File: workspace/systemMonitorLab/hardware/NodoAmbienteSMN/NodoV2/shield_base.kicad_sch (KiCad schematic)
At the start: 18 parts, among them J1 Molex_MainBoard_DHT22, J2 Molex_MainBoard_BMP280, J3 Jack-DC, J6 Molex_MainBoard_Led_Status, Q1 Q_NPN_BEC, Q2 Q_NPN_BEC, Q3 Q_NPN_BEC, Q4 Q_NPN_BEC, U1 NodeMcuEsp8266

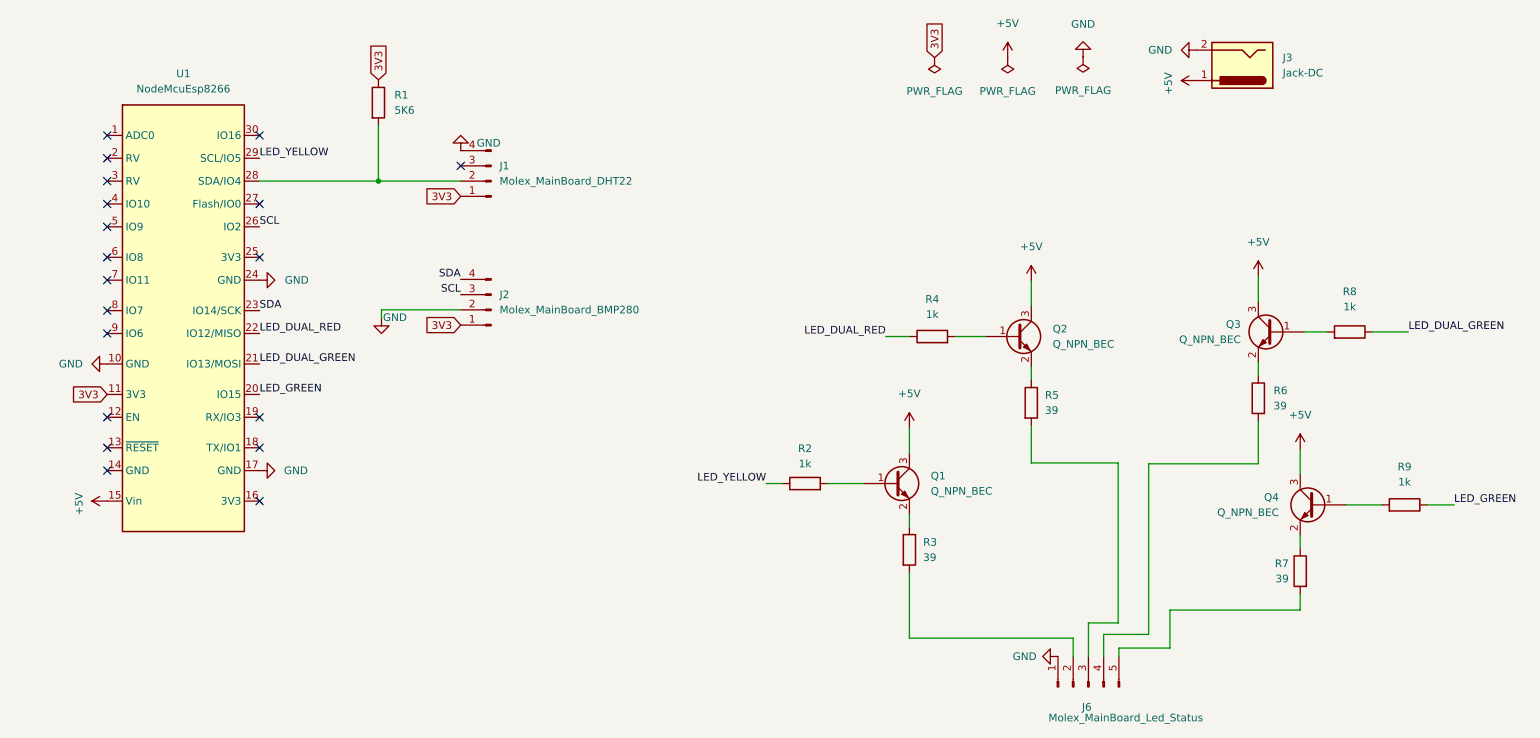
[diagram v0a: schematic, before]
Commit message: Se termino de generar el diseño de la placa shield_main_board.
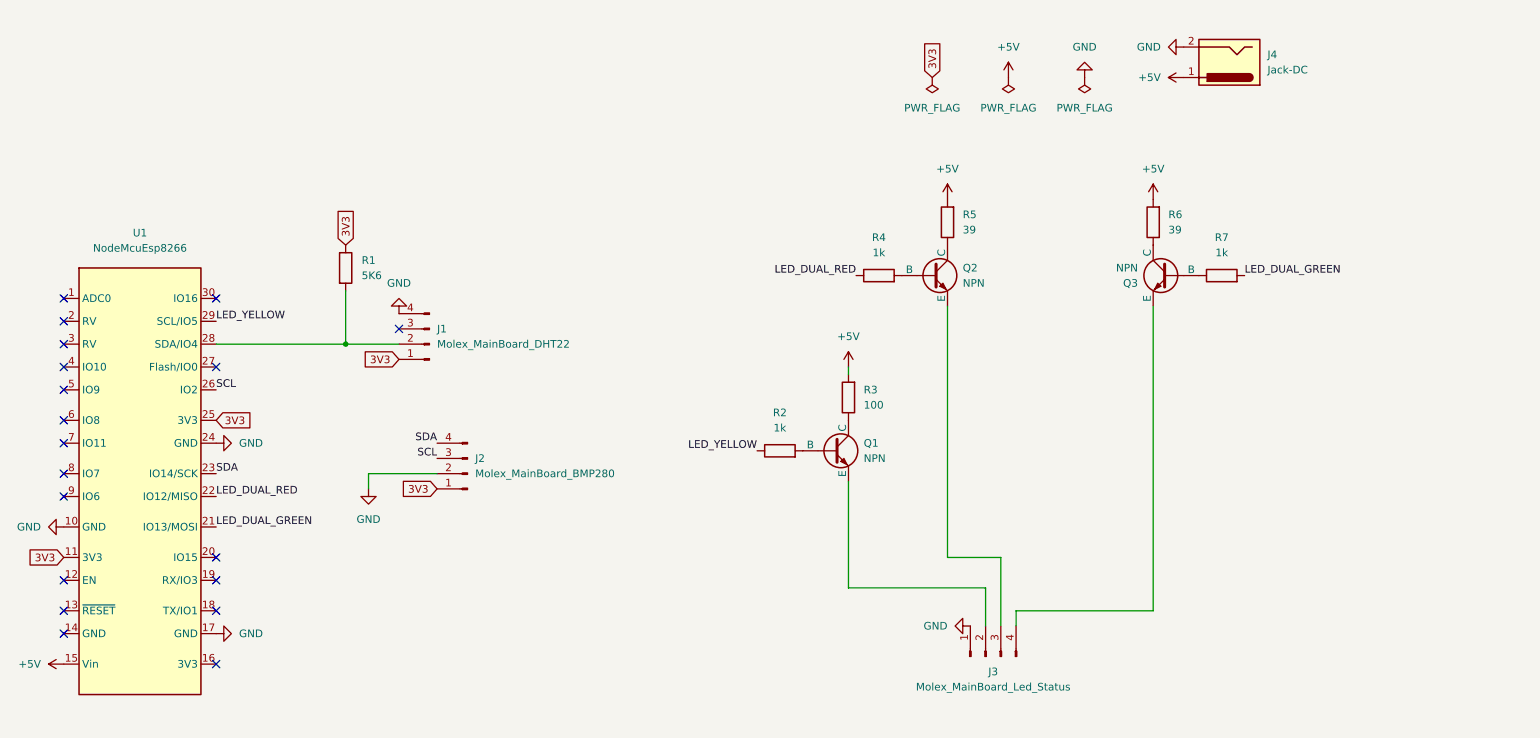
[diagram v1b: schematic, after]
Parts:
- removed J1: Molex_MainBoard_DHT22, Connector_PinHeader_2.54mm:PinHeader_1x04_P2.54mm_Horizontal, symbol Connector:Conn_01x04_Male
- removed J2: Molex_MainBoard_BMP280, Connector_PinHeader_2.54mm:PinHeader_1x04_P2.54mm_Horizontal, symbol Connector:Conn_01x04_Male
- removed J3: Jack-DC, Connector_BarrelJack:BarrelJack_GCT_DCJ200-10-A_Horizontal, symbol Connector:Jack-DC
- removed J6: Molex_MainBoard_Led_Status, Connector_PinHeader_2.54mm:PinHeader_1x05_P2.54mm_Horizontal, symbol Connector:Conn_01x05_Male
- removed Q1, Q2, Q3, Q4: Q_NPN_BEC, Package_TO_SOT_SMD:SOT-23, symbol Device:Q_NPN_BEC
- removed R8, R9: 1k, Resistor_SMD:R_1206_3216Metric, symbol Device:R
- removed U1: NodeMcuEsp8266, NodeMCU_Module:ESP8266_v3, symbol New_Library:NodeMcuEsp8266
- added J1: Molex_MainBoard_DHT22, Connector_PinHeader_2.54mm:PinHeader_1x04_P2.54mm_Horizontal, symbol Connector:Conn_01x04_Pin
- added J2: Molex_MainBoard_BMP280, Connector_PinHeader_2.54mm:PinHeader_1x04_P2.54mm_Horizontal, symbol Connector:Conn_01x04_Pin
- added J3: Molex_MainBoard_Led_Status, Connector_PinHeader_2.54mm:PinHeader_1x04_P2.54mm_Horizontal, symbol Connector:Conn_01x04_Pin
- added J4: Jack-DC, Connector_BarrelJack:BarrelJack_Horizontal, symbol Connector:Jack-DC
- added Q1, Q2, Q3: NPN, Package_TO_SOT_SMD:SOT-23, symbol Simulation_SPICE:NPN
- added U1: NodeMcuEsp8266, Module_commercial:ESP8266_v3, symbol Modulos_comerciales:NodeMcuEsp8266
- R3: value 39 -> 100
- R7: value 39 -> 1k
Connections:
- net +5V: now also R3.2, R5.2, R6.2, J4.1, U1.15 (Vin)
- net 3V3: now also J1.1 (Pin_1), J2.1 (Pin_1), U1.11 (3V3), U1.25 (3V3)
- net GND: now also J1.4 (Pin_4), J2.2 (Pin_2), J3.1 (Pin_1), J4.2, U1.10 (GND), U1.17 (GND), U1.24 (GND)
- net LED_DUAL_GREEN: now also R7.2, U1.21 (IO13/MOSI)
- net LED_DUAL_RED: now also U1.22 (IO12/MISO)
- net LED_YELLOW: now also U1.29 (SCL/IO5)
- net SCL: now also J2.3 (Pin_3), U1.26 (IO2)
- net SDA: now also J2.4 (Pin_4), U1.23 (IO14/SCK)
- net at R3.1: now also Q1.1 (C)
- net at R7.1: now also Q3.2 (B)
- net at R6.1: now also Q3.1 (C)
- net at R4.2: now also Q2.2 (B)
- net at R1.2: now also J1.2 (Pin_2), U1.28 (SDA/IO4)
- net at R5.1: now also Q2.1 (C)
- net at R2.2: now also Q1.2 (B)
- new net: J3.4 (Pin_4), Q3.3 (E)
- new net: J3.3 (Pin_3), Q2.3 (E)
- new net: J3.2 (Pin_2), Q1.3 (E)
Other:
- company: Servicio Meteorologico Argentino (SMN) -> Servicio Meteorológico Nacional (SMN)
- moved on the sheet: R1

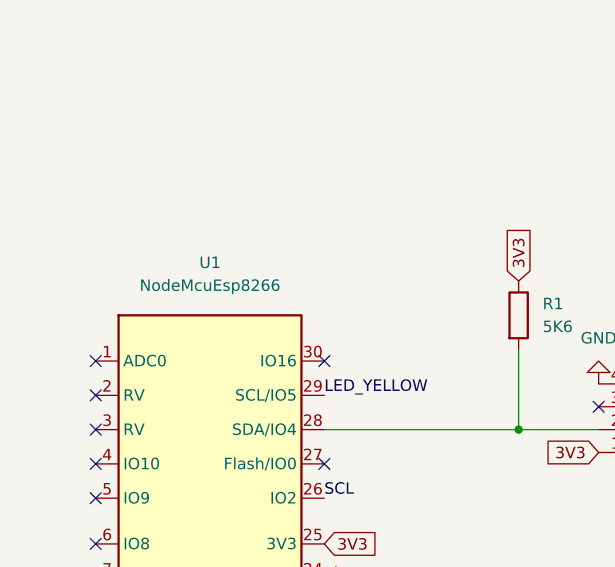
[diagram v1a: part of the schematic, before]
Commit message: Actulizamos pcbs de nodo ambiente v2
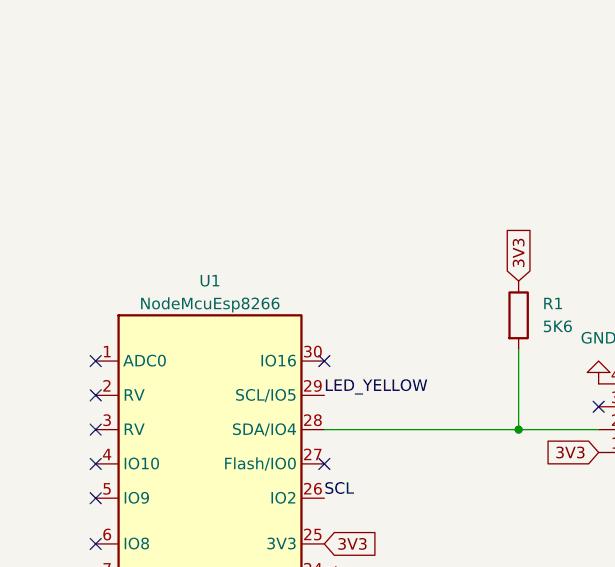
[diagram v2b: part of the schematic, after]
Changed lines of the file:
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@@
 		(fields_autoplaced yes)
 		(property "Reference" "U1"
-			(at 49.53 58.928 0)
+			(at 49.53 60.96 0)
 			(effects
 				(font
@@
 		)
 		(property "Value" "NodeMcuEsp8266"
-			(at 49.53 61.468 0)
+			(at 49.53 63.5 0)
 			(effects
 				(font
@@
 					(size 1.27 1.27)
 				)
+				(hide yes)
 			)
 		)
 		(pin "1"
 		)
-		(pin "10"
-		)
-		(pin "11"
-		)
-		(pin "12"
-		)
-		(pin "13"
-		)
-		(pin "14"
-		)
-		(pin "15"
-		)
-		(pin "16"
-		)
-		(pin "17"
-		)
-		(pin "18"
-		)
-		(pin "19"
-		)
 		(pin "2"
 		)
-		(pin "20"
-		)
-		(pin "21"
-		)
-		(pin "22"
-		)
-		(pin "23"
-		)
-		(pin "24"
-		)
-		(pin "25"
-		)
-		(pin "26"
-		)
-		(pin "27"
-		)
-		(pin "28"
-		)
-		(pin "29"
-		)
 		(pin "3"
-		)
-		(pin "30"
 		)
 		(pin "4"
@@
 		(pin "6"
 		)
-		(pin "7"
+		(pin "10"
 		)
 		(pin "8"
 		)
+		(pin "20"
+		)
+		(pin "29"
+		)
+		(pin "7"
+		)
+		(pin "28"
+		)
+		(pin "22"
+		)
+		(pin "30"
+		)
+		(pin "21"
+		)
+		(pin "19"
+		)
+		(pin "11"
+		)
+		(pin "26"
+		)
+		(pin "12"
+		)
+		(pin "25"
+		)
+		(pin "17"
+		)
+		(pin "15"
+		)
+		(pin "23"
+		)
+		(pin "16"
+		)
+		(pin "27"
+		)
+		(pin "18"
+		)
 		(pin "9"
 		)
+		(pin "24"
+		)
+		(pin "13"
+		)
+		(pin "14"
+		)
 		(instances

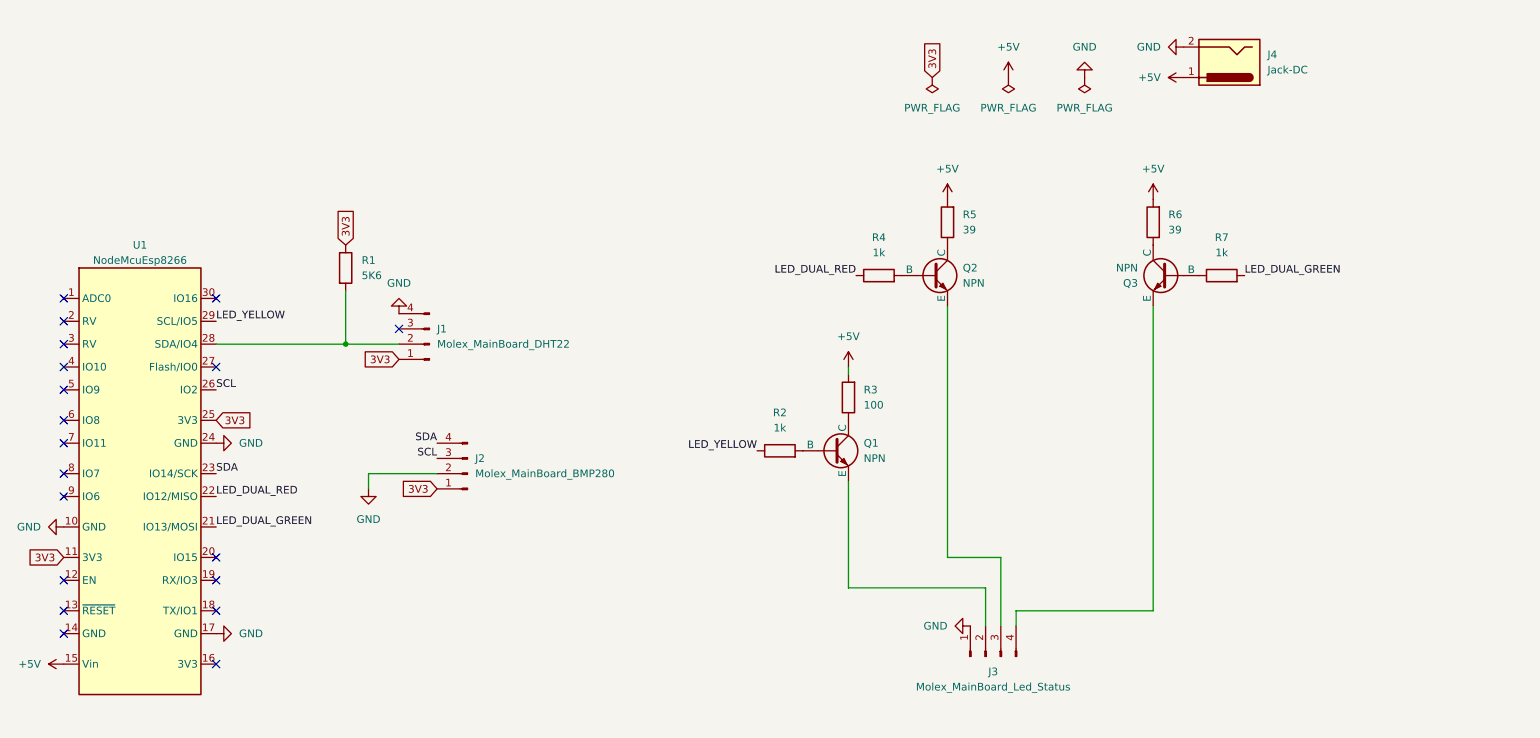
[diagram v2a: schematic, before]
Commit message: Vamos agregando la lista proveedores a la lista de componentes
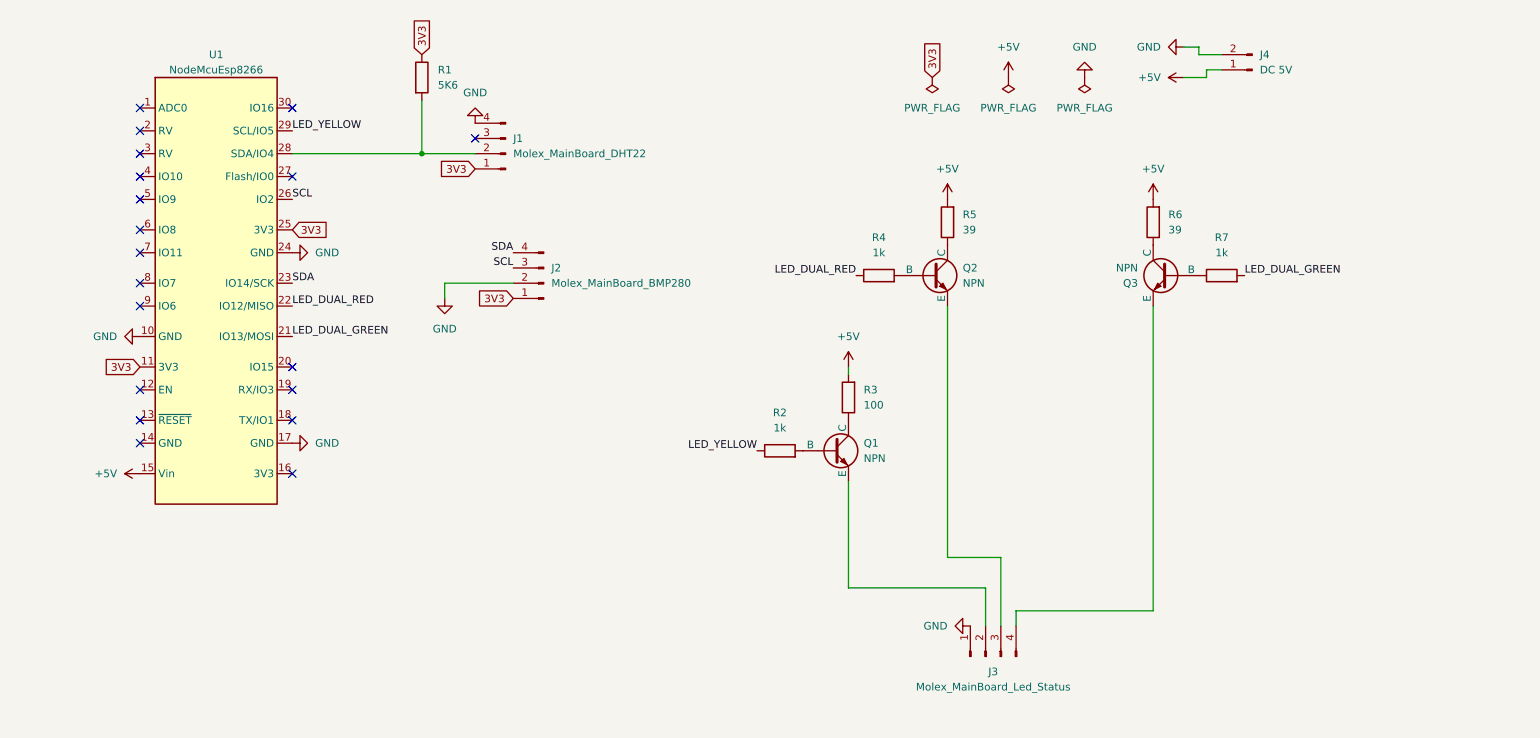
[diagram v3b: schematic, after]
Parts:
- removed J4: Jack-DC, Connector_BarrelJack:BarrelJack_Horizontal, symbol Connector:Jack-DC
- added J4: DC 5V, Connector_PinHeader_2.54mm:PinHeader_1x02_P2.54mm_Horizontal, symbol Connector:Conn_01x02_Pin
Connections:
- net +5V: now also J4.1 (Pin_1)
- net GND: now also J4.2 (Pin_2)
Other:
- moved on the sheet: J1, J2, R1, U1

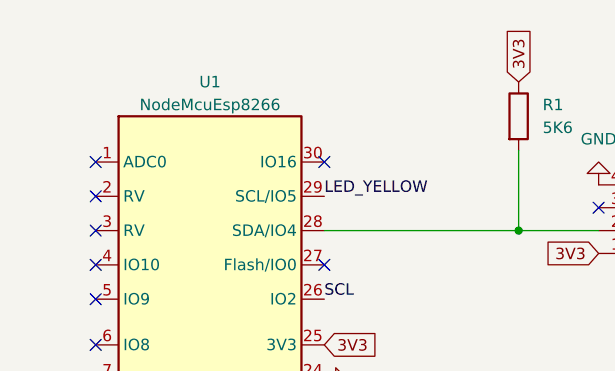
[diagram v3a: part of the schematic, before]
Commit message: Se mejora el plano de masa del PCB
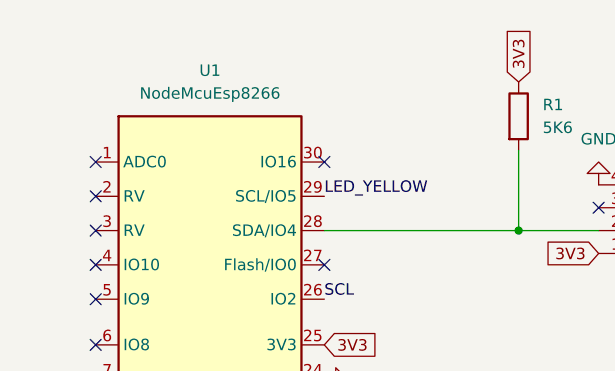
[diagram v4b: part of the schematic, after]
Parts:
- removed U1: NodeMcuEsp8266, Module_commercial:ESP8266_v3, symbol Modulos_comerciales:NodeMcuEsp8266
- added U1: NodeMcuEsp8266, Modulos_comerciales:ESP8266_v3, symbol simbolos:NodeMcuEsp8266
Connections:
- net +5V: now also U1.15 (Vin)
- net 3V3: now also U1.11 (3V3), U1.25 (3V3)
- net GND: now also U1.10 (GND), U1.17 (GND), U1.24 (GND)
- net LED_DUAL_GREEN: now also U1.21 (IO13/MOSI)
- net LED_DUAL_RED: now also U1.22 (IO12/MISO)
- net LED_YELLOW: now also U1.29 (SCL/IO5)
- net SCL: now also U1.26 (IO2)
- net SDA: now also U1.23 (IO14/SCK)
- net at J1.2 (Pin_2), R1.2: now also U1.28 (SDA/IO4)
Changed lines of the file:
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@@
+	)
+	(symbol
+		(lib_id "simbolos:NodeMcuEsp8266")
+		(at 223.52 245.11 0)
+		(unit 1)
+		(exclude_from_sim no)
+		(in_bom yes)
+		(on_board yes)
+		(dnp no)
+		(fields_autoplaced yes)
+		(property "Reference" "U1"
+			(at 62.23 27.94 0)
+			(effects
+				(font
+					(size 1.27 1.27)
+				)
+			)
+		)
+		(property "Value" "NodeMcuEsp8266"
+			(at 62.23 30.48 0)
+			(effects
+				(font
+					(size 1.27 1.27)
+				)
+			)
+		)
+		(property "Footprint" "Modulos_comerciales:ESP8266_v3"
+			(at 62.23 118.11 0)
+			(effects
+				(font
+					(size 1.27 1.27)
+				)
+				(hide yes)
+			)
+		)
+		(property "Datasheet" ""
+			(at 21.59 124.46 0)
+			(effects
+				(font
+					(size 1.27 1.27)
+				)
+				(hide yes)
+			)
+		)
+		(property "Description" ""
+			(at 223.52 245.11 0)
+			(effects
+				(font
+					(size 1.27 1.27)
+				)
+				(hide yes)
+			)
+		)
+		(pin "27"
+		)
+		(pin "8"
+		)
+		(pin "30"
+		)
+		(pin "22"
+		)
+		(pin "18"
+		)
+		(pin "23"
+		)
+		(pin "15"
+		)
+		(pin "11"
+		)
+		(pin "28"
+		)
+		(pin "14"
+		)
+		(pin "20"
+		)
+		(pin "3"
+		)
+		(pin "4"
+		)
+		(pin "6"
+		)
+		(pin "2"
+		)
+		(pin "10"
+		)
+		(pin "5"
+		)
+		(pin "13"
+		)
+		(pin "24"
+		)
+		(pin "1"
+		)
+		(pin "7"
+		)
+		(pin "9"
+		)
+		(pin "12"
+		)
+		(pin "29"
+		)
+		(pin "26"
+		)
+		(pin "25"
+		)
+		(pin "19"
+		)
+		(pin "21"
+		)
+		(pin "17"
+		)
+		(pin "16"
+		)
+		(instances
+			(project ""
+				(path "/31567b71-44a6-4f20-978f-6760a129c7a5/38d5e957-879e-408c-8450-ff788dcea95c"
+					(reference "U1")
+					(unit 1)
+				)
+			)
+		)
 	)
 	(symbol
@@
 					(unit 1)
 				)
-			)
-		)
-	)
-	(symbol
-		(lib_id "Modulos_comerciales:NodeMcuEsp8266")
-		(at 223.52 245.11 0)
-		(unit 1)
-		(exclude_from_sim no)
-		(in_bom yes)
-		(on_board yes)
-		(dnp no)
-		(fields_autoplaced yes)
-		(property "Reference" "U1"
-			(at 62.23 29.21 0)
-			(effects
-				(font
-					(size 1.27 1.27)
-				)
-			)
-		)
-		(property "Value" "NodeMcuEsp8266"
-			(at 62.23 31.75 0)
-			(effects
-				(font
-					(size 1.27 1.27)
-				)
-			)
-		)
-		(property "Footprint" "Module_commercial:ESP8266_v3"
-			(at 62.23 118.11 0)
-			(effects
-				(font
-					(size 1.27 1.27)
-				)
-				(hide yes)
-			)
-		)
-		(property "Datasheet" ""
-			(at 21.59 124.46 0)
-			(effects
-				(font
-					(size 1.27 1.27)
-				)
-				(hide yes)
-			)
-		)
-		(property "Description" ""
-			(at 223.52 245.11 0)
-			(effects
-				(font
-					(size 1.27 1.27)
-				)
-				(hide yes)
-			)
-		)
-		(pin "1"
-		)
-		(pin "2"
-		)
-		(pin "3"
-		)
-		(pin "4"
-		)
-		(pin "5"
-		)
-		(pin "6"
-		)
-		(pin "10"
-		)
-		(pin "8"
-		)
-		(pin "20"
-		)
-		(pin "29"
-		)
-		(pin "7"
-		)
-		(pin "28"
-		)
-		(pin "22"
-		)
-		(pin "30"
-		)
-		(pin "21"
-		)
-		(pin "19"
-		)
-		(pin "11"
-		)
-		(pin "26"
-		)
-		(pin "12"
-		)
-		(pin "25"
-		)
-		(pin "17"
-		)
-		(pin "15"
-		)
-		(pin "23"
-		)
-		(pin "16"
-		)
-		(pin "27"
-		)
-		(pin "18"
-		)
-		(pin "9"
-		)
-		(pin "24"
-		)
-		(pin "13"
-		)
-		(pin "14"
-		)
-		(instances
-			(project ""
-				(path "/31567b71-44a6-4f20-978f-6760a129c7a5/38d5e957-879e-408c-8450-ff788dcea95c"
-					(reference "U1")
-					(unit 1)
-				)
